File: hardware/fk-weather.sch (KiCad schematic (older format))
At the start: 77 parts, among them J1 MICRO-USB, J2 CONN_01X03, J6 CONN-HDR-2x5, M1 MOUNT_HOLE, M2 MOUNT_HOLE, M3 MOUNT_HOLE, M4 MOUNT_HOLE, P101 CONN_01X05, Q1 2N7002LT1G, Q2 2N7002LT1G, Q3 2N7002LT1G, SW1 SPNO, U1 ATSAMD21G18A-AU, U101 TSL2591, U102 MPL3115A2, U103 BNO055, U104 SHT31, U2 MCP1700T-XXX2E, U3 MAX4466, Y1 FC-135, Y101 FC-135

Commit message: Fixing footprints for light and pressure.
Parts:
- U101: footprint Housings_DFN_QFN:DFN-6-1.3x1.2mm_Pitch0.4mm -> Housings_DFN_QFN:DFN-6-1EP_2x2mm_Pitch0.65mm
- U102: footprint Housings_DFN_QFN:DFN-8_2x2mm_Pitch0.5mm -> conservify:DFN-8-1EP_5x2.55mm_Pitch1.25mm_98ASA002260D
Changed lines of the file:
@@
 EESchema Schematic File Version 2
 LIBS:fk-weather-rescue
-LIBS:conservify
-LIBS:RocketScreamKicadLibrary
-LIBS:conn
-LIBS:74xgxx
-LIBS:74xx
-LIBS:ac-dc
-LIBS:actel
-LIBS:adc-dac
-LIBS:allegro
-LIBS:Altera
-LIBS:analog_devices
-LIBS:analog_switches
-LIBS:atmel
-LIBS:audio
-LIBS:battery_management
-LIBS:bbd
-LIBS:bosch
-LIBS:brooktre
-LIBS:cmos_ieee
-LIBS:cmos4000
-LIBS:contrib
-LIBS:cypress
-LIBS:dc-dc
-LIBS:device
-LIBS:digital-audio
-LIBS:diode
-LIBS:display
-LIBS:dsp
-LIBS:elec-unifil
-LIBS:ESD_Protection
-LIBS:ftdi
-LIBS:gennum
-LIBS:graphic
-LIBS:hc11
-LIBS:intel
-LIBS:interface
-LIBS:ir
-LIBS:Lattice
-LIBS:leds
-LIBS:linear
-LIBS:logo
-LIBS:maxim
-LIBS:mechanical
-LIBS:memory
-LIBS:microchip
-LIBS:microchip_dspic33dsc
-LIBS:microchip_pic10mcu
-LIBS:microchip_pic12mcu
-LIBS:microchip_pic16mcu
-LIBS:microchip_pic18mcu
-LIBS:microchip_pic24mcu
-LIBS:microchip_pic32mcu
-LIBS:microcontrollers
-LIBS:modules
-LIBS:motor_drivers
-LIBS:motorola
-LIBS:motors
-LIBS:msp430
-LIBS:nordicsemi
-LIBS:nxp
-LIBS:nxp_armmcu
-LIBS:onsemi
-LIBS:opto
-LIBS:Oscillators
-LIBS:philips
-LIBS:power
-LIBS:Power_Management
-LIBS:powerint
-LIBS:pspice
-LIBS:references
-LIBS:regul
-LIBS:relays
-LIBS:rfcom
-LIBS:sensors
-LIBS:silabs
-LIBS:siliconi
-LIBS:stm8
-LIBS:stm32
-LIBS:supertex
-LIBS:switches
-LIBS:texas
-LIBS:transf
-LIBS:transistors
-LIBS:triac_thyristor
-LIBS:ttl_ieee
-LIBS:valves
-LIBS:video
-LIBS:wiznet
-LIBS:Worldsemi
-LIBS:Xicor
-LIBS:xilinx
-LIBS:zetex
-LIBS:Zilog
 LIBS:fk-weather-cache
 EELAYER 25 0
@@
 F 0 "U102" H 9600 1550 60  0000 C CNN
 F 1 "MPL3115A2" H 9600 1650 60  0000 C CNN
-F 2 "Housings_DFN_QFN:DFN-8_2x2mm_Pitch0.5mm" H 9600 1550 60  0001 C CNN
+F 2 "conservify:DFN-8-1EP_5x2.55mm_Pitch1.25mm_98ASA002260D" H 9600 1550 60  0001 C CNN
 F 3 "" H 9600 1550 60  0001 C CNN
 F 4 "841-MPL3115A2" H -400 -300 50  0001 C CNN "spn1"
@@
 F 0 "U101" H 9500 3150 60  0000 C CNN
 F 1 "TSL2591" H 9500 3250 60  0000 C CNN
-F 2 "Housings_DFN_QFN:DFN-6-1.3x1.2mm_Pitch0.4mm" H 9500 3150 60  0001 C CNN
+F 2 "Housings_DFN_QFN:DFN-6-1EP_2x2mm_Pitch0.65mm" H 9500 3150 60  0001 C CNN
 F 3 "" H 9500 3150 60  0001 C CNN
 F 4 "985-TSL25911FN" H -350 -450 50  0001 C CNN "spn1"

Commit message: Fixing USB oval drills.
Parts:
- J1: footprint RocketScreamKicadLibrary:MICRO-USB -> conservify:MICRO-USB
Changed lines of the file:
@@
 F 0 "J1" H 4650 10250 60  0000 C CNN
 F 1 "MICRO-USB" H 4650 9550 60  0000 C CNN
-F 2 "RocketScreamKicadLibrary:MICRO-USB" H 4650 9450 60  0001 C CNN
+F 2 "conservify:MICRO-USB" H 4650 9450 60  0001 C CNN
 F 3 "" H 4700 10100 60  0000 C CNN
 	1    4650 9900

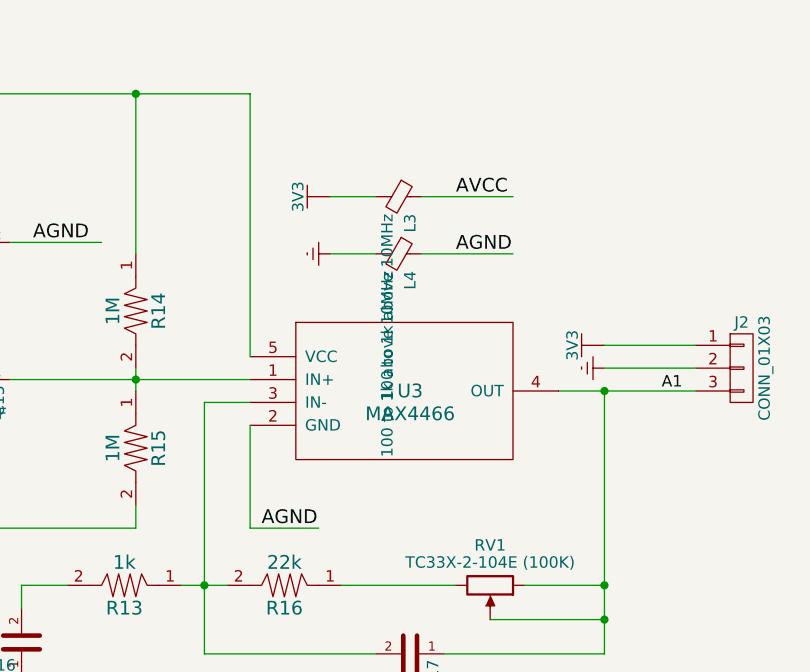
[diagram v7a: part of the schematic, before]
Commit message: Arranging labels for printing out an assembly map.
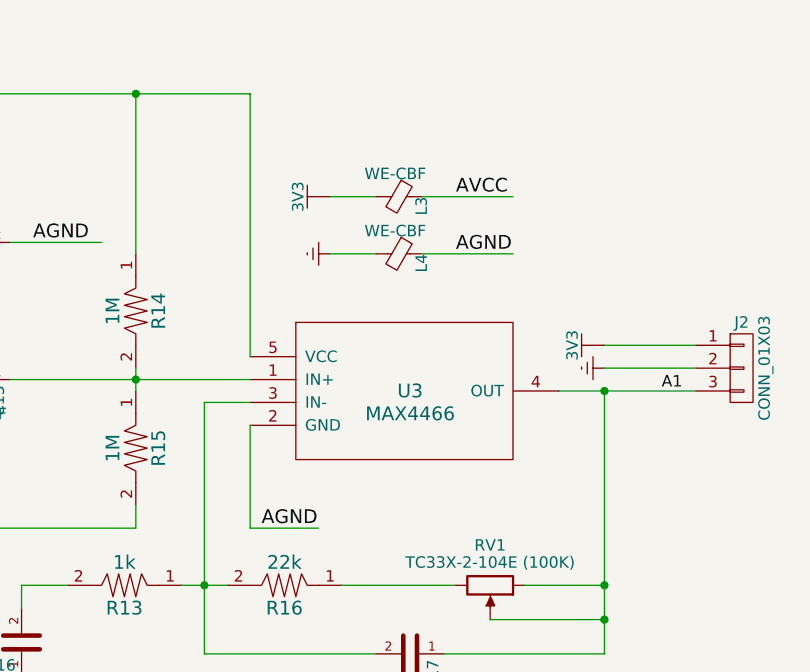
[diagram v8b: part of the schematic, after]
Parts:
- L3, L4: value 100 to 1k above 10MHz -> WE-CBF
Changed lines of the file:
@@
 U 1 1 597B1AF6
 P 13650 7100
-F 0 "L3" H 13725 7150 50  0000 L CNN
-F 1 "100 to 1k above 10MHz" H 13725 7050 50  0000 L CNN
+F 0 "L3" H 13650 7200 50  0000 L CNN
+F 1 "WE-CBF" V 13550 6950 50  0000 L CNN
 F 2 "Resistors_SMD:R_0603_HandSoldering" V 13580 7100 50  0001 C CNN
 F 3 "" H 13650 7100 50  0001 C CNN
@@
 U 1 1 597B1C32
 P 13650 7350
-F 0 "L4" H 13725 7400 50  0000 L CNN
-F 1 "100 to 1k above 10MHz" H 13725 7300 50  0000 L CNN
+F 0 "L4" H 13650 7450 50  0000 L CNN
+F 1 "WE-CBF" V 13550 7200 50  0000 L CNN
 F 2 "Resistors_SMD:R_0603_HandSoldering" V 13580 7350 50  0001 C CNN
 F 3 "" H 13650 7350 50  0001 C CNN
